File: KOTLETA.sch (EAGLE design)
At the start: 106 parts, among them CON1 SM06B-SRSS-TB, CON2 CON-4P-JST_GH-RA, CON3 CON-4P-JST_GH-RA, IC1 STM32F105RCT6, IC2 CAT24C02, IC3 SN65HVD232D, IC4 LMR14010ADDCT, IC5 LM75BD-TSSOP8, IC6 FAN7888, IC7 ZXCT1051, IC8 3.3V, Q1 CSD18510Q5B, Q2 CSD18510Q5B, Q3 CSD18510Q5B, Q4 CSD18510Q5B, Q5 CSD18510Q5B, Q6 CSD18510Q5B, X1 24MHz

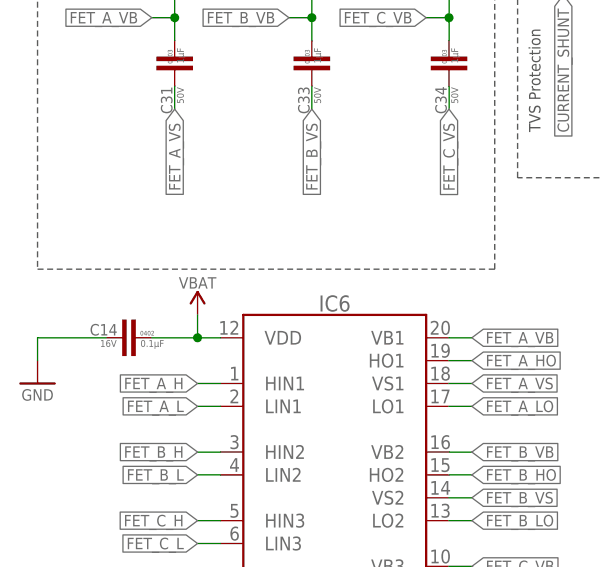
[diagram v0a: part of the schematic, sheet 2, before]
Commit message: proper gitignore
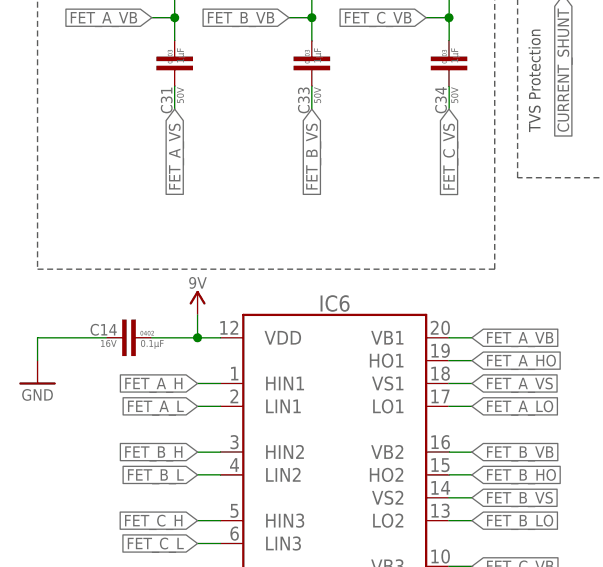
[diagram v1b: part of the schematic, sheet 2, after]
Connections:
- net VBAT: no longer C14.1, IC6.VDD
- net VDD_9V: now also C14.1, IC6.VDD
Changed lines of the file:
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@@
 <part name="+P3" library="supply_symbols" library_urn="urn:adsk.eagle:library:5017758" deviceset="VBAT" device=""/>
 <part name="+P4" library="supply_symbols" library_urn="urn:adsk.eagle:library:5017758" deviceset="VBAT" device=""/>
-<part name="+P5" library="supply_symbols" library_urn="urn:adsk.eagle:library:5017758" deviceset="VBAT" device=""/>
 <part name="C36" library="C_digikey" library_urn="urn:adsk.eagle:library:2539367" deviceset="22µF" device="-1206" package3d_urn="urn:adsk.eagle:package:2539382/2" technology="-35V_20%_X5R" value="22µF"/>
 <part name="GND16" library="sapog_reference_hardware" deviceset="GND" device=""/>
@@
 <part name="C38" library="C_digikey" library_urn="urn:adsk.eagle:library:2539367" deviceset="22µF" device="-1206" package3d_urn="urn:adsk.eagle:package:2539382/2" technology="-35V_20%_X5R" value="22µF"/>
 <part name="GND33" library="sapog_reference_hardware" deviceset="GND" device=""/>
+<part name="+P12" library="supply_symbols" library_urn="urn:adsk.eagle:library:5017758" deviceset="9V" device=""/>
 </parts>
 <sheets>
@@
 <attribute name="VALUE" x="246.38" y="168.656" size="1.27" layer="96" font="vector" ratio="15" align="center"/>
 </instance>
-<instance part="+P5" gate="G$1" x="25.4" y="121.92" smashed="yes">
-<attribute name="VALUE" x="25.4" y="125.476" size="1.27" layer="96" font="vector" ratio="15" align="center"/>
-</instance>
 <instance part="C36" gate="G$1" x="144.78" y="81.28" smashed="yes" rot="MR270">
 <attribute name="NAME" x="145.669" y="80.01" size="1.27" layer="95" rot="MR270" align="center-left"/>
@@
 <instance part="GND33" gate="1" x="149.86" y="71.12" smashed="yes">
 <attribute name="VALUE" x="149.86" y="69.85" size="1.27" layer="96" font="vector" ratio="15" align="center"/>
+</instance>
+<instance part="+P12" gate="G$1" x="25.4" y="121.92" smashed="yes">
+<attribute name="VALUE" x="25.4" y="125.476" size="1.27" layer="96" font="vector" ratio="15" align="center"/>
 </instance>
 </instances>
@@
 </segment>
 <segment>
-<pinref part="IC6" gate="G$1" pin="VDD"/>
-<pinref part="C14" gate="G$1" pin="1"/>
-<wire x1="20.32" y1="119.38" x2="25.4" y2="119.38" width="0.1524" layer="91"/>
-<pinref part="+P5" gate="G$1" pin="VBAT"/>
-<wire x1="25.4" y1="119.38" x2="27.94" y2="119.38" width="0.1524" layer="91"/>
-<wire x1="25.4" y1="121.92" x2="25.4" y2="119.38" width="0.1524" layer="91"/>
-<junction x="25.4" y="119.38"/>
-</segment>
-<segment>
 <pinref part="D3" gate="G$1" pin="A"/>
 <wire x1="22.86" y1="165.1" x2="22.86" y2="167.64" width="0.1524" layer="91"/>
@@
 <junction x="149.86" y="86.36"/>
 </segment>
-</net>
+<segment>
+<pinref part="IC6" gate="G$1" pin="VDD"/>
+<pinref part="C14" gate="G$1" pin="1"/>
+<wire x1="20.32" y1="119.38" x2="25.4" y2="119.38" width="0.1524" layer="91"/>
+<wire x1="25.4" y1="119.38" x2="27.94" y2="119.38" width="0.1524" layer="91"/>
+<wire x1="25.4" y1="121.92" x2="25.4" y2="119.38" width="0.1524" layer="91"/>
+<junction x="25.4" y="119.38"/>
+<pinref part="+P12" gate="G$1" pin="VDD_9V"/>
+</segment>
+</net>

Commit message: routing done
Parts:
- C28: device C_digikey:1µF-10V_10%_X7R-0603 -> C_digikey:1µF-10V_10%_X5R-0603
- R14: value 0.005 OHM -> 0.005R; device sapog_reference_hardware:CURRENT_SHUNT-CSNL2010 -> SHUNT_RESISTORS:CURRENT_SHUNT_KELVIN-0.005R-2010-KELVIN
- X1: device GNSS2_master_lib:CRYSTAL-3.2X2.5-4P -> crystal:CRYSTAL-4P-24MHZ-3.2X2.5-4P
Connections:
- net CURRENT_SHUNT: now also R14.1; no longer R14.C1
- net GND: now also R14.2; no longer R14.C2
- net GNDD: no longer IC3.NC@1
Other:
- moved on the sheet: C11, C37, IC3

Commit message: updates
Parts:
- CON1: value SM06B-SRSS-TB -> CON-6P; device sapog_reference_hardware:SM06B-SRSS-TB -> Connectors:CON-6P
- IC2: device sapog_reference_hardware:CAT24C02 -> misc:CAT24C02
- IC5: device sapog_reference_hardware:LM75BD-TSSOP8 -> misc:LM75BD-TSSOP8
- IC8: device sapog_reference_hardware:NCV1117-3.3 -> linear regulators:NCV1117-3.3
- LED1: device sapog_reference_hardware:LTST-C19HE1WT -> myxa_masterlib:LTST-C19HE1WT
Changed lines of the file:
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@@
 </part>
 <part name="C13" library="C_digikey" library_urn="urn:adsk.eagle:library:2539367" deviceset="0.1µF" device="-0402" package3d_urn="urn:adsk.eagle:package:2539379/2" technology="-16V_10%_X7R" value="0.1µF"/>
-<part name="IC6" library="mosfet_drivers" library_urn="urn:adsk.eagle:library:7691028" deviceset="FAN7888" device="" package3d_urn="urn:adsk.eagle:package:7544831/1">
+<part name="IC6" library="mosfet_drivers" library_urn="urn:adsk.eagle:library:7691028" deviceset="FAN7888" device="" package3d_urn="urn:adsk.eagle:package:7544831/2">
 <attribute name="PARTNO" value="FAN7888MX"/>
 </part>
-<part name="CON1" library="sapog_reference_hardware" deviceset="SM06B-SRSS-TB" device="">
+<part name="CON1" library="Connectors" library_urn="urn:adsk.eagle:library:3750510" deviceset="CON-6P" device="" package3d_urn="urn:adsk.eagle:package:1041174/4">
 <attribute name="PARTNO" value="SM06B-SRSS-TB"/>
 </part>
@@
 <part name="R2" library="R_digikey" library_urn="urn:adsk.eagle:library:2539499" deviceset="3K9" device="-0402" package3d_urn="urn:adsk.eagle:package:2539512/2" technology="-1%" value="3K9"/>
 <part name="R3" library="R_digikey" library_urn="urn:adsk.eagle:library:2539499" deviceset="3K9" device="-0402" package3d_urn="urn:adsk.eagle:package:2539512/2" technology="-1%" value="3K9"/>
-<part name="IC5" library="sapog_reference_hardware" deviceset="LM75BD" device="-TSSOP8"/>
+<part name="IC5" library="misc" library_urn="urn:adsk.eagle:library:5347860" deviceset="LM75BD" device="-TSSOP8" package3d_urn="urn:adsk.eagle:package:7691413/3"/>
 <part name="P+13" library="sapog_reference_hardware" deviceset="3.3V" device=""/>
 <part name="GND17" library="sapog_reference_hardware" deviceset="GND" device=""/>
 <part name="GND20" library="sapog_reference_hardware" deviceset="GND" device=""/>
 <part name="GND25" library="sapog_reference_hardware" deviceset="GND" device=""/>
-<part name="LED1" library="sapog_reference_hardware" deviceset="LTST-C19HE1WT" device=""/>
+<part name="LED1" library="myxa_masterlib" library_urn="urn:adsk.eagle:library:1040030" deviceset="LTST-C19HE1WT" device="" package3d_urn="urn:adsk.eagle:package:1040199/2"/>
 <part name="P+8" library="sapog_reference_hardware" deviceset="3.3V" device=""/>
 <part name="C29" library="C_digikey" library_urn="urn:adsk.eagle:library:2539367" deviceset="4.7µF" device="-0603" package3d_urn="urn:adsk.eagle:package:2539381/2" technology="-6.3V_10%_X7R" value="4.7µF"/>
-<part name="IC8" library="sapog_reference_hardware" deviceset="NCV1117-3.3" device="" value="3.3V"/>
+<part name="IC8" library="linear regulators" library_urn="urn:adsk.eagle:library:2541155" deviceset="NCV1117-3.3" device="" package3d_urn="urn:adsk.eagle:package:8637283/1" value="3.3V"/>
 <part name="GND5" library="sapog_reference_hardware" deviceset="GND" device=""/>
 <part name="GND7" library="sapog_reference_hardware" deviceset="GND" device=""/>
@@
 <part name="C34" library="C_digikey" library_urn="urn:adsk.eagle:library:2539367" deviceset="1µF" device="-0603" package3d_urn="urn:adsk.eagle:package:2539381/2" technology="-50V_10%_X7R" value="1µF"/>
 <part name="GND34" library="sapog_reference_hardware" deviceset="GND" device=""/>
-<part name="IC7" library="misc" library_urn="urn:adsk.eagle:library:5347860" deviceset="ZXCT1051" device="" package3d_urn="urn:adsk.eagle:package:5347863/5"/>
+<part name="IC7" library="misc" library_urn="urn:adsk.eagle:library:5347860" deviceset="ZXCT1051" device="" package3d_urn="urn:adsk.eagle:package:5347863/6"/>
 <part name="GND11" library="sapog_reference_hardware" deviceset="GND" device=""/>
 <part name="GND10" library="sapog_reference_hardware" deviceset="GND" device=""/>
@@
 <part name="P+6" library="sapog_reference_hardware" deviceset="3.3V" device=""/>
 <part name="P+7" library="sapog_reference_hardware" deviceset="3.3V" device=""/>
-<part name="IC2" library="sapog_reference_hardware" deviceset="CAT24C02" device=""/>
+<part name="IC2" library="misc" library_urn="urn:adsk.eagle:library:5347860" deviceset="CAT24C02" device="" package3d_urn="urn:adsk.eagle:package:5347863/6"/>
 <part name="GND9" library="sapog_reference_hardware" deviceset="GND" device=""/>
 <part name="C10" library="C_digikey" library_urn="urn:adsk.eagle:library:2539367" deviceset="0.1µF" device="-0402" package3d_urn="urn:adsk.eagle:package:2539379/2" technology="-16V_10%_X7R" value="0.1µF"/>

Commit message: Updates
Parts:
- removed R28: (no value), rc:R-1%-0402
- added PAD1, PAD10, PAD11, PAD12, PAD13, PAD14, PAD15, PAD16, PAD17, PAD18, PAD19, PAD2, PAD3, PAD4, PAD5, PAD6, PAD7, PAD8, PAD9: PAD-HOLE-0.6, PADS:PAD-HOLE-0.6
- added R29: 200R, R_digikey:200R-5%-0402
- added R30: 10K, R_digikey:10K-0.1%-0402
- R27: value (none) -> 130K; DIGIKEY# (none) -> YAG2969CT-ND; MANF (none) -> Yageo; MANF# (none) -> RC0402FR-07130KL
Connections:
- new net N$15: IC1.PC1, R29.1
- net FET_A_VS: now also PAD17.P$1, PAD7.P$1, PAD8.P$1
- net FET_B_VS: now also PAD10.P$1, PAD18.P$1, PAD9.P$1
- net FET_C_VS: now also PAD11.P$1, PAD12.P$1, PAD19.P$1
- net GND: now also PAD4.P$1, PAD5.P$1, PAD6.P$1, R30.1; no longer IC1.PC1, R28.1
- net GNDD: now also PAD13.P$1
- net N$22: now also PAD16.P$1
- net N$23: now also PAD15.P$1
- net N$24: now also R30.2; no longer R28.2
- net N$25: now also PAD14.P$1
- net VBAT: now also PAD1.P$1, PAD2.P$1, PAD3.P$1
- net VDD_3V3: now also R29.2
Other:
- note added: "Feedback voltage 0.74 0.765 0.79"
- note added: "Set feedback voltage divider ratio with VOUT = VFB (1+(R27/R28))."
- note added: "Vout min = 10.36 Vout = 10.71 Vout max = 11.06"
- moved on the sheet: A, B, C, C24, C30, C32, CON1, Q1, Q2, Q3, Q4, Q5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

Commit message: BOM fixes
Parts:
- C28: device C_digikey:1µF-10V_10%_X5R-0603 -> C_digikey:1µF-50V_10%_X7R-0603
- C4: device C_digikey:1µF-10V_10%_X7R-0603 -> C_digikey:1µF-50V_10%_X7R-0603
- R1, R26, R29: ASSEMBLY DNM -> (none)
- R14: value 0.005R -> 0.001R; device SHUNT_RESISTORS:CURRENT_SHUNT_KELVIN-0.005R-2010-KELVIN -> SHUNT_RESISTORS:CURRENT_SHUNT_KELVIN-0.001R-2010-KELVIN
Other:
- note added: "WP pin pull up is optional"

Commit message: comments
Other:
- note added: "https://docs.google.com/spreadsheets/d/1WwElBVsDBB5yf-5zQ-RQBamWm7rKtQzdxvj4nXSMxlk/edit?usp=sharing"
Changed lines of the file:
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@@
 Vout = 10.71
 Vout max = 11.06</text>
+<text x="78.74" y="52.07" size="0.635" layer="97">https://docs.google.com/spreadsheets/d/1WwElBVsDBB5yf-5zQ-RQBamWm7rKtQzdxvj4nXSMxlk/edit?usp=sharing</text>
 </plain>
 <instances>
